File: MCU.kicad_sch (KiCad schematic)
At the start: 29 parts, among them J1 TagConnect, J2 Conn_ARM_JTAG_SWD_10, U1 nRF52833_QDxx, Y1 32MHz, Y2 32.768k

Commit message: schematic capture like half done, need to do a lot of the smaller things
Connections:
- net GND: now also C9.2
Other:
- note added: "TO:DO: - Figure out RF Rules area for ERC/DRC - NFC - LED Component Selection - BLE antenna selection - Test pads"
- note removed: "TO:DO: - Figure out RF Rules area for ERC/DRC - NFC - LED Component Selection"
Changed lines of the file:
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@@
 		)
 	)
-	(text "TO:DO:\n- Figure out RF Rules area for ERC/DRC\n- NFC\n- LED Component Selection"
+	(text "TO:DO:\n- Figure out RF Rules area for ERC/DRC\n- NFC\n- LED Component Selection\n- BLE antenna selection\n- Test pads"
 		(exclude_from_sim no)
 		(at 13.208 16.51 0)
@@
 	)
 	(junction
+		(at 60.96 49.53)
+		(diameter 0)
+		(color 0 0 0 0)
+	)
+	(junction
 		(at 43.18 69.85)
 		(diameter 0)
@@
 	)
 	(junction
+		(at 86.36 24.13)
+		(diameter 0)
+		(color 0 0 0 0)
+	)
+	(junction
 		(at 144.78 31.75)
 		(diameter 0)
@@
 	(wire
 		(pts
+			(xy 95.25 24.13) (xy 86.36 24.13)
+		)
+		(stroke
+			(width 0)
+			(type default)
+		)
+	)
+	(wire
+		(pts
 			(xy 58.42 158.75) (xy 63.5 158.75)
 		)
@@
 	(wire
 		(pts
-			(xy 63.5 50.8) (xy 63.5 49.53)
+			(xy 60.96 50.8) (xy 60.96 49.53)
 		)
 		(stroke
@@
 	(wire
 		(pts
+			(xy 95.25 22.86) (xy 95.25 24.13)
+		)
+		(stroke
+			(width 0)
+			(type default)
+		)
+	)
+	(wire
+		(pts
 			(xy 81.28 16.51) (xy 83.82 16.51)
 		)
@@
 	(symbol
 		(lib_id "power:GND")
-		(at 63.5 50.8 0)
+		(at 60.96 50.8 0)
 		(unit 1)
 		(body_style 1)
@@
 		(fields_autoplaced yes)
 		(property "Reference" "#PWR07"
-			(at 63.5 57.15 0)
+			(at 60.96 57.15 0)
 			(hide yes)
 			(show_name no)
@@
 		)
 		(property "Value" "GND"
-			(at 63.5 55.88 0)
+			(at 60.96 55.88 0)
 			(show_name no)
 			(do_not_autoplace no)
@@
 		)
 		(property "Footprint" ""
-			(at 63.5 50.8 0)
+			(at 60.96 50.8 0)
 			(hide yes)
 			(show_name no)
@@
 		)
 		(property "Datasheet" ""
-			(at 63.5 50.8 0)
+			(at 60.96 50.8 0)
 			(hide yes)
 			(show_name no)
@@
 		)
 		(property "Description" "Power symbol creates a global label with name \"GND\" , ground"
-			(at 63.5 50.8 0)
+			(at 60.96 50.8 0)
 			(hide yes)
 			(show_name no)

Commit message: all schematic done but RF
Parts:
- removed C14: 12p, symbol Device:C_Small
- removed Y1: 32MHz, Crystal:Crystal_SMD_2016-4Pin_2.0x1.6mm, symbol Device:Crystal_GND24
- added AE1: NFC, symbol Device:Antenna_Loop
- added C41, C42: TBD, Capacitor_SMD:C_0402_1005Metric, symbol Device:C_Small
- added R14, R15: 0R, Resistor_SMD:R_0402_1005Metric, symbol Device:R_Small_US
- added TP15: MOSI, symbol Connector:TestPoint
- added TP16: MISO, symbol Connector:TestPoint
- added TP17: SCK, symbol Connector:TestPoint
- added TP18: SDA, symbol Connector:TestPoint
- added TP19: SCL, symbol Connector:TestPoint
- added TP20: CS_IMU, symbol Connector:TestPoint
- added TP21: CS_DW, symbol Connector:TestPoint
- added Y1: 32MHz, Oscillator:Oscillator_SMD_ECS_2520MV-xxx-xx-4Pin_2.5x2.0mm, symbol Oscillator:ECS-2520MV-xxx-xx
- C1, C10, C11, C12, C15, C16, C17, C18, C2, C3, C4, C5, C6, C7, C8, C9: footprint (none) -> Capacitor_SMD:C_0402_1005Metric
- C13: value 12p -> 0.1u; footprint (none) -> Capacitor_SMD:C_0402_1005Metric
- D3: value TBD -> BLUE; footprint (none) -> LED_SMD:LED_0603_1608Metric
- L1: footprint (none) -> Inductor_SMD:L_0603_1608Metric
- L2, L3, L4: footprint (none) -> Inductor_SMD:L_0402_1005Metric
- R6: value TBD -> 330; footprint (none) -> Resistor_SMD:R_0603_1608Metric
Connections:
- net +1V8: now also C13.1, Y1.4 (VDD)
- net CS_DW: now also TP21.1
- net CS_IMU: now also TP20.1
- net GND: now also C13.2, C41.2, C42.1, Y1.2 (GND); no longer C13.1, R6.2
- net LED: now also R6.2; no longer D3.2 (A)
- net MISO: now also TP16.1
- net MOSI: now also TP15.1
- net NFC1: now also C42.2, R14.1
- net NFC2: now also C41.1, R15.1
- net SCK: now also TP17.1
- net SCL: now also TP19.1
- net SDA: now also TP18.1
- net at U1.28 (XC1): now also Y1.3 (OUT); no longer C13.2
- net ANT renamed ANT_BLE
- new net: AE1.1, R14.2
- new net: AE1.2, R15.2
- new net VSYS: D3.2 (A)
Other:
- note added: "BLE - 2.4G"
- note added: "NFC - 13.56M"
- note added: "TO:DO: - NFC FE & antenna selection - BLE antenna selection"
- note removed: "NFC"
- note removed: "RF"
- note removed: "TO:DO: - Figure out RF Rules area for ERC/DRC - NFC - LED Component Selection - BLE antenna selection - Test pads"
- moved on the sheet: D3, R6

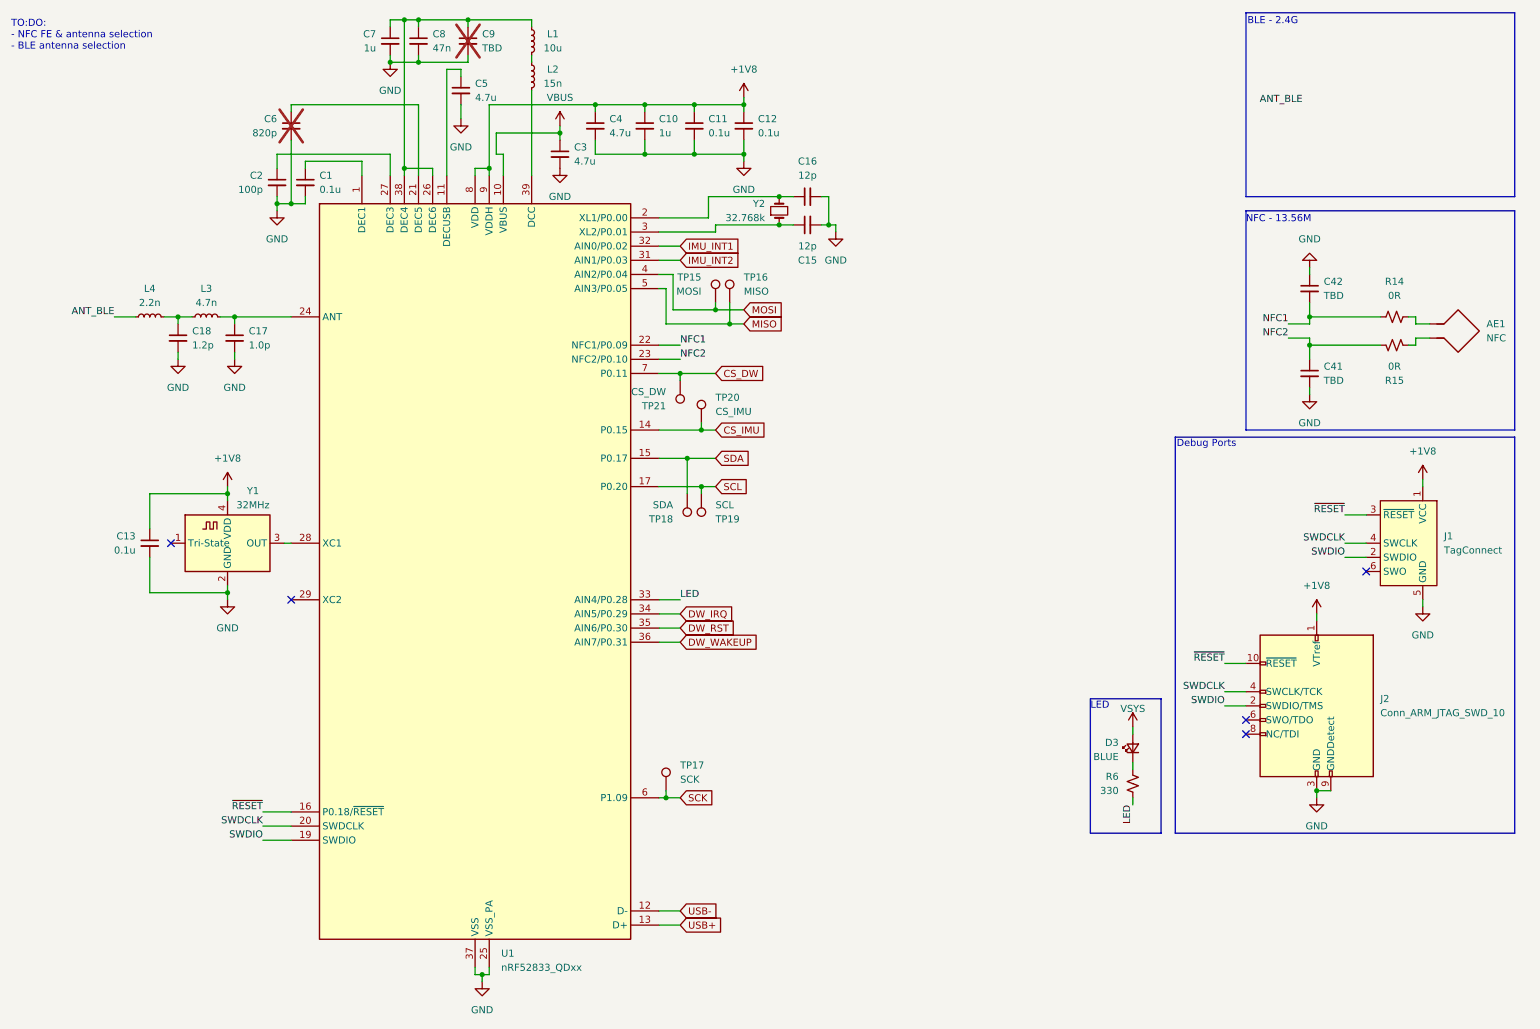
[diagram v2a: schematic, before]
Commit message: schematic & bom done except for UWB RF
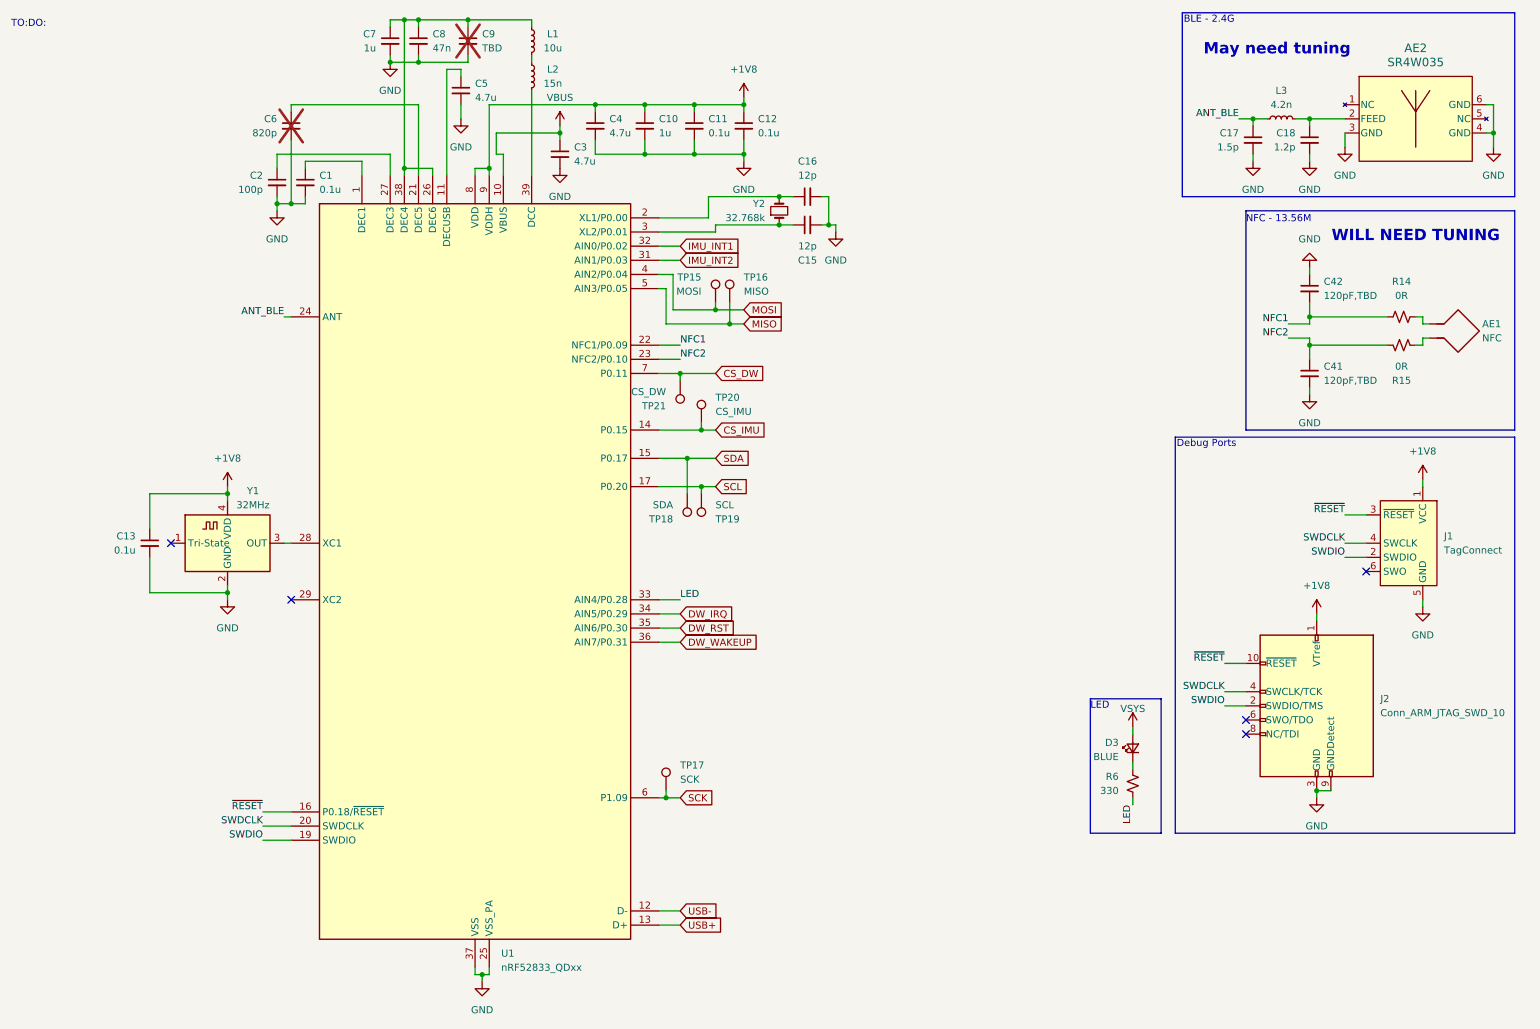
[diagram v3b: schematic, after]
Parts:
- removed L4: 2.2n, Inductor_SMD:L_0402_1005Metric, symbol Device:L_Small
- added AE2: SR4W035, TrActor:SR4W035_4X6_ANT, symbol TrActor:SR4W035
- AE1: footprint (none) -> TrActor:NFC-Coil
- C17: value 1.0p -> 1.5p
- C41, C42: value TBD -> 120pF,TBD
- L3: value 4.7n -> 4.2n
- TP15, TP16, TP17, TP18, TP19, TP20, TP21: footprint (none) -> TestPoint:TestPoint_Pad_D1.5mm
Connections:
- net ANT_BLE: now also C17.1, L3.2, U1.24 (ANT)
- net GND: now also AE2.3 (GND), AE2.4 (GND), AE2.6 (GND)
- net at C18.1, L3.1: now also AE2.2 (FEED)
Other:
- note added: "May need tuning"
- note added: "TO:DO:"
- note added: "WILL NEED TUNING"
- note removed: "TO:DO: - NFC FE & antenna selection - BLE antenna selection"
- moved on the sheet: R14, R15

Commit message: routing started
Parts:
- J2: value Conn_ARM_JTAG_SWD_10 -> Debug
- R6: footprint Resistor_SMD:R_0603_1608Metric -> Resistor_SMD:R_0402_1005Metric
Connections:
- net at C7.1, C8.1, C9.1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: now also L2.2; no longer L1.1
- net at U1.39 (DCC): now also L1.1; no longer L2.2
- net at AE1.1, R14.2: now also C42.2
- net at AE1.2, R15.2: now also C41.1
- net NFC1 renamed NFC+
- net NFC+: no longer C42.2
- net NFC2 renamed NFC-
- net NFC-: no longer C41.1
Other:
- note added: "BLE - 2.4GHz"
- note added: "I stole these passive values from a similar application with the same MCU & antenna made by someone who's smarter than me. We'll see how well they work."
- note added: "Initial build will not place the two 0R resistors. Antenna will be tuned via the resistor's pads. Shunt capacitors will be used to make antenna resonate at 13.56MHz, then the resistors will be placed. Future boards will place the correct capacitors and resistors by default."
- note added: "NFC - 13.56MHz"
- note removed: "BLE - 2.4G"
- note removed: "NFC - 13.56M"
- moved on the sheet: C3, C41, C42, C5, L1, L2

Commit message: routing hell
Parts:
- TP15, TP16, TP17, TP18, TP19, TP20, TP21: footprint TestPoint:TestPoint_Pad_D1.5mm -> TestPoint:TestPoint_Pad_D1.0mm
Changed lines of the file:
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@@
 			)
 		)
-		(property "Footprint" "TestPoint:TestPoint_Pad_D1.5mm"
+		(property "Footprint" "TestPoint:TestPoint_Pad_D1.0mm"
 			(at 142.24 88.9 0)
 			(hide yes)
@@
 			)
 		)
-		(property "Footprint" "TestPoint:TestPoint_Pad_D1.5mm"
+		(property "Footprint" "TestPoint:TestPoint_Pad_D1.0mm"
 			(at 139.7 101.6 0)
 			(hide yes)
@@
 			)
 		)
-		(property "Footprint" "TestPoint:TestPoint_Pad_D1.5mm"
+		(property "Footprint" "TestPoint:TestPoint_Pad_D1.0mm"
 			(at 142.24 101.6 0)
 			(hide yes)
@@
 			)
 		)
-		(property "Footprint" "TestPoint:TestPoint_Pad_D1.5mm"
+		(property "Footprint" "TestPoint:TestPoint_Pad_D1.0mm"
 			(at 128.27 81.28 0)
 			(hide yes)
@@
 			)
 		)
-		(property "Footprint" "TestPoint:TestPoint_Pad_D1.5mm"
+		(property "Footprint" "TestPoint:TestPoint_Pad_D1.0mm"
 			(at 134.62 67.31 0)
 			(hide yes)
@@
 			)
 		)
-		(property "Footprint" "TestPoint:TestPoint_Pad_D1.5mm"
+		(property "Footprint" "TestPoint:TestPoint_Pad_D1.0mm"
 			(at 135.89 154.94 0)
 			(hide yes)
@@
 			)
 		)
-		(property "Footprint" "TestPoint:TestPoint_Pad_D1.5mm"
+		(property "Footprint" "TestPoint:TestPoint_Pad_D1.0mm"
 			(at 147.32 67.31 0)
 			(hide yes)

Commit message: ready for DR
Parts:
- removed R14, R15: 0R, Resistor_SMD:R_0402_1005Metric, symbol Device:R_Small_US
- AE1: footprint TrActor:NFC-Coil -> TrActor:AANI-CH-0029
- C41, C42: value 120pF,TBD -> 8pF
- C6, C9: now left out of the parts list
- J2: footprint Connector_PinHeader_1.27mm:PinHeader_2x05_P1.27mm_Vertical_SMD -> Connector_PinHeader_1.27mm:PinHeader_2x05_P1.27mm_Vertical
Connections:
- net CS_DW: now also U1.4 (AIN2/P0.04); no longer U1.7 (P0.11)
- net DW_IRQ: now also U1.36 (AIN7/P0.31); no longer U1.34 (AIN5/P0.29)
- net DW_RST: now also U1.34 (AIN5/P0.29); no longer U1.35 (AIN6/P0.30)
- net DW_WAKEUP: now also U1.35 (AIN6/P0.30); no longer U1.36 (AIN7/P0.31)
- net IMU_INT1: now also U1.31 (AIN1/P0.03); no longer U1.32 (AIN0/P0.02)
- net IMU_INT2: now also U1.32 (AIN0/P0.02); no longer U1.31 (AIN1/P0.03)
- net MOSI: now also U1.6 (P1.09); no longer U1.4 (AIN2/P0.04)
- net NFC+: now also AE1.1, C42.2
- net NFC-: now also AE1.2, C41.1
- net SCK: now also U1.7 (P0.11); no longer U1.6 (P1.09)
- net BLE_ANT: now reaches AE2.2 (FEED), C18.1, L3.1
- net ANT_BLE renamed RF_BLE
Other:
- note added: "This is a guess that doesn't account for the PCB"
- note removed: "Initial build will not place the two 0R resistors. Antenna will be tuned via the resistor's pads. Shunt capacitors will be used to make antenna resonate at 13.56MHz, then the resistors will be placed. Future boards will place the correct capacitors and resistors by default."
- note removed: "WILL NEED TUNING"

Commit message: ordering commit fr
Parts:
- TP15, TP16, TP17, TP18, TP19, TP20, TP21: now left out of the parts list
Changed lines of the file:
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@@
 		(body_style 1)
 		(exclude_from_sim no)
-		(in_bom yes)
+		(in_bom no)
 		(on_board yes)
 		(in_pos_files yes)
@@
 		(body_style 1)
 		(exclude_from_sim no)
-		(in_bom yes)
+		(in_bom no)
 		(on_board yes)
 		(in_pos_files yes)
@@
 		(body_style 1)
 		(exclude_from_sim no)
-		(in_bom yes)
+		(in_bom no)
 		(on_board yes)
 		(in_pos_files yes)
@@
 		(body_style 1)
 		(exclude_from_sim no)
-		(in_bom yes)
+		(in_bom no)
 		(on_board yes)
 		(in_pos_files yes)
@@
 		(body_style 1)
 		(exclude_from_sim no)
-		(in_bom yes)
+		(in_bom no)
 		(on_board yes)
 		(in_pos_files yes)
@@
 		(body_style 1)
 		(exclude_from_sim no)
-		(in_bom yes)
+		(in_bom no)
 		(on_board yes)
 		(in_pos_files yes)
@@
 		(body_style 1)
 		(exclude_from_sim no)
-		(in_bom yes)
+		(in_bom no)
 		(on_board yes)
 		(in_pos_files yes)
